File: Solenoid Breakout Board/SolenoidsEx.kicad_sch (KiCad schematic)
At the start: 80 parts, among them Q10 IRF540N, Q11 IRF540N, Q12 IRF540N, Q13 IRF540N, Q14 IRF540N, Q15 IRF540N, Q16 IRF540N, Q17 IRF540N, Q18 IRF540N, Q19 IRF540N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

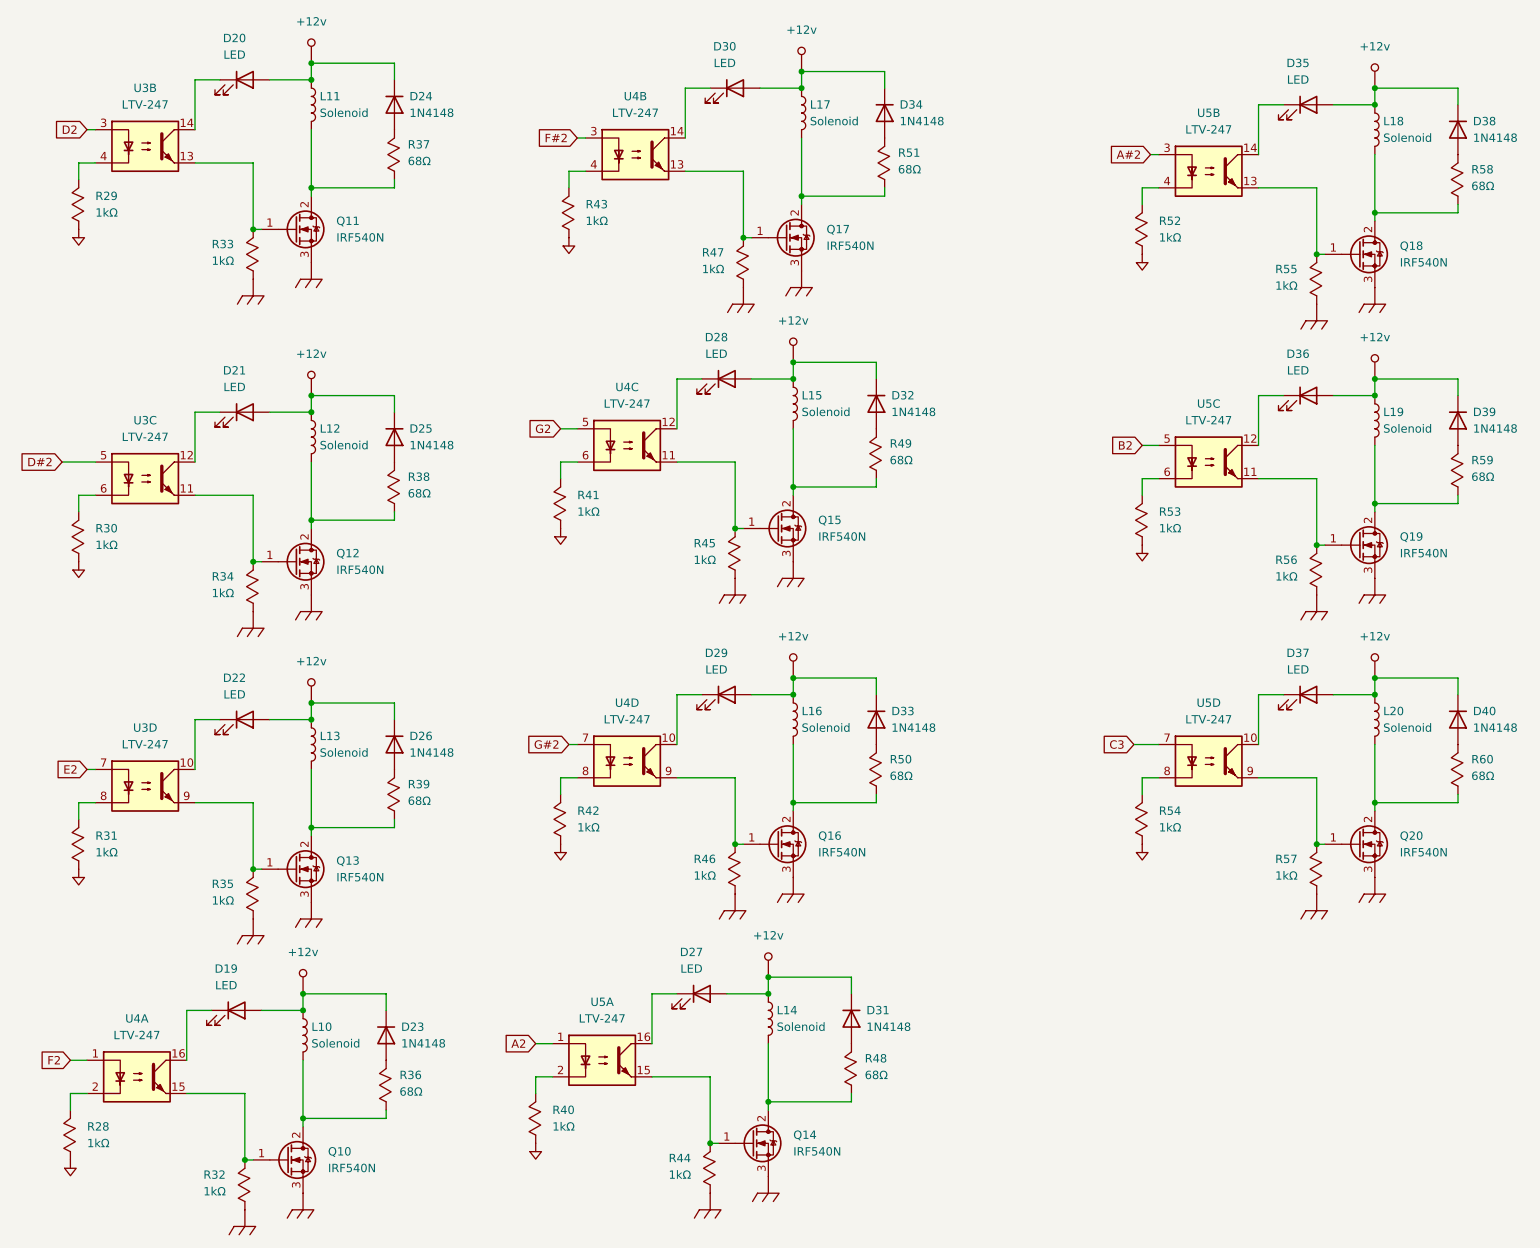
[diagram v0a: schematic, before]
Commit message: replaced footprints on breakout to match new components
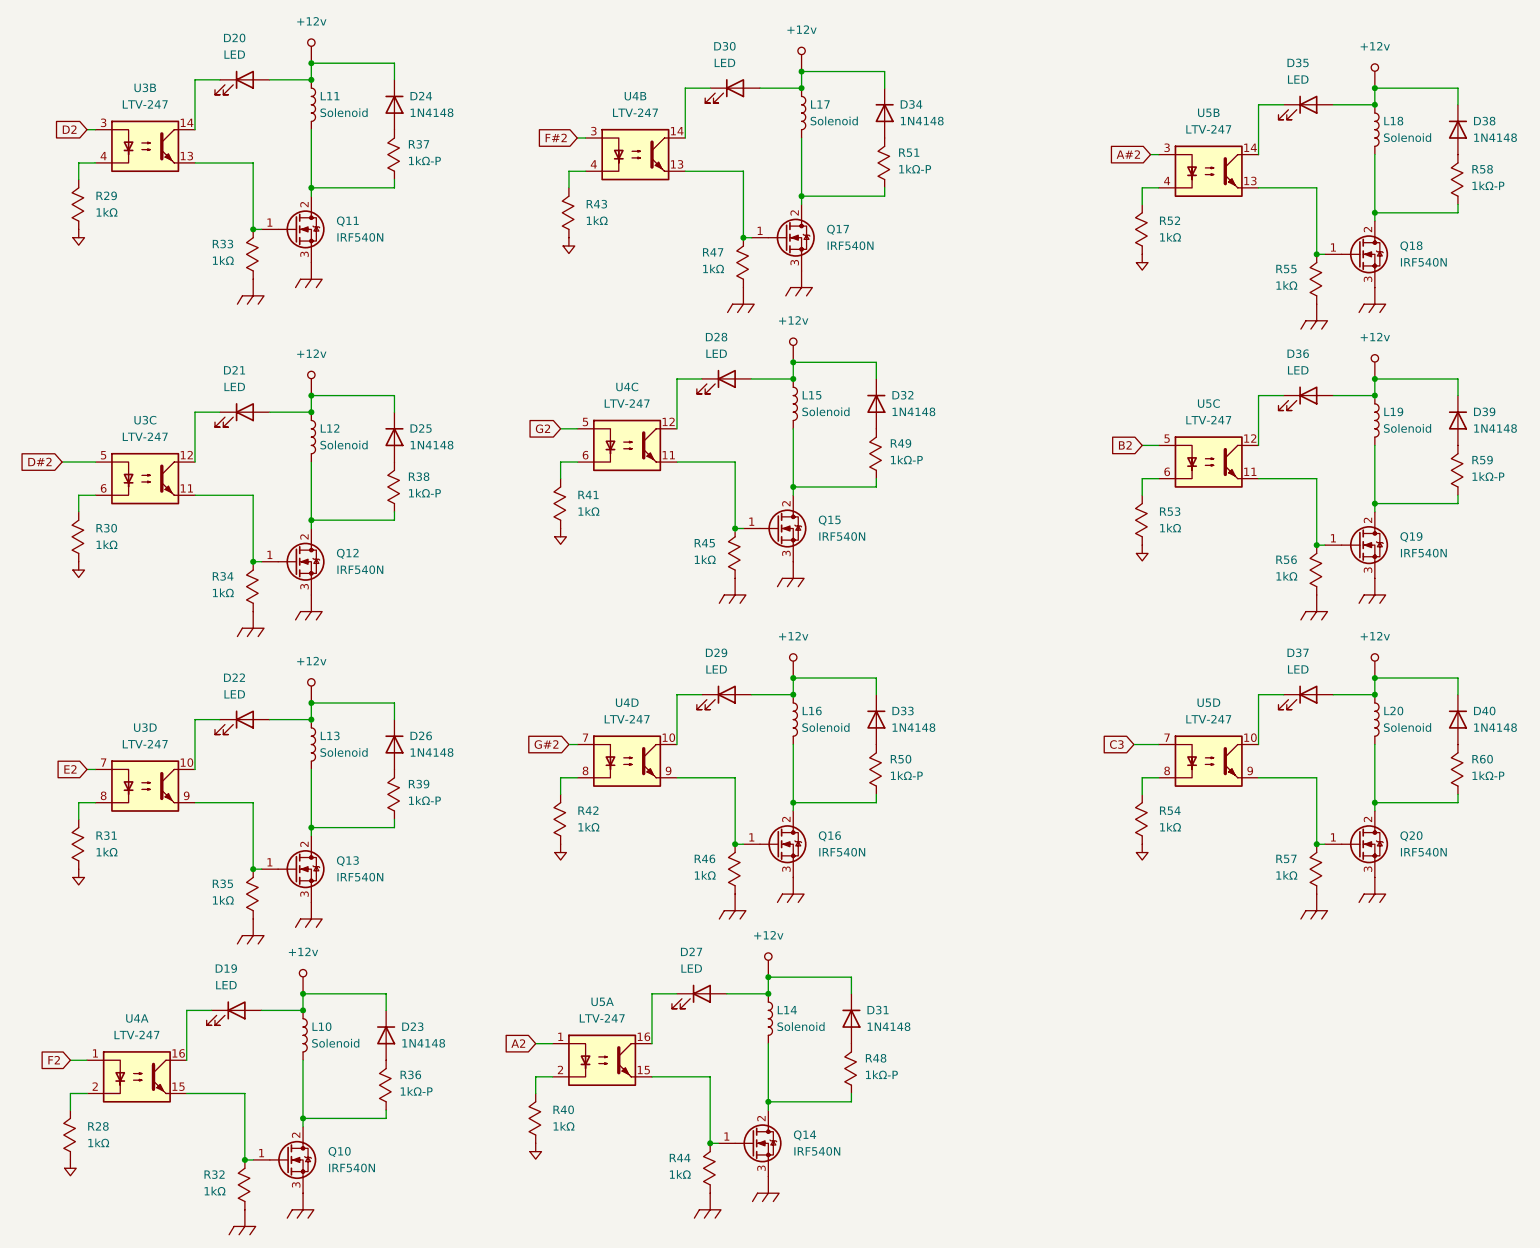
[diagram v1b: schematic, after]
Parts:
- Q10, Q11, Q12, Q13, Q14, Q15, Q16, Q17, Q18, Q19, Q20: footprint Package_TO_SOT_THT:TO-220-3_Vertical -> Package_TO_SOT_THT:TO-220-3_Horizontal_TabUp
- R36, R37, R38, R39, R48, R49, R50, R51, R58, R59, R60: value 68Ω -> 1kΩ-P; footprint Resistor_SMD:R_0805_2012Metric_Pad1.20x1.40mm_HandSolder -> Resistor_SMD:R_1206_3216Metric_Pad1.30x1.75mm_HandSolder
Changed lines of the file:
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@@
 			)
 		)
-		(property "Value" "68Ω"
+		(property "Value" "1kΩ-P"
 			(at 71.882 180.086 90)
 			(effects
@@
 			)
 		)
-		(property "Footprint" "Resistor_SMD:R_0805_2012Metric_Pad1.20x1.40mm_HandSolder"
+		(property "Footprint" "Resistor_SMD:R_1206_3216Metric_Pad1.30x1.75mm_HandSolder"
 			(at 67.31 180.34 0)
 			(effects
@@
 			)
 		)
-		(property "Footprint" "Package_TO_SOT_THT:TO-220-3_Vertical"
+		(property "Footprint" "Package_TO_SOT_THT:TO-220-3_Horizontal_TabUp"
 			(at 134.62 95.885 0)
 			(effects
@@
 			)
 		)
-		(property "Value" "68Ω"
+		(property "Value" "1kΩ-P"
 			(at 73.152 37.846 90)
 			(effects
@@
 			)
 		)
-		(property "Footprint" "Resistor_SMD:R_0805_2012Metric_Pad1.20x1.40mm_HandSolder"
+		(property "Footprint" "Resistor_SMD:R_1206_3216Metric_Pad1.30x1.75mm_HandSolder"
 			(at 68.58 38.1 0)
 			(effects
@@
 			)
 		)
-		(property "Value" "68Ω"
+		(property "Value" "1kΩ-P"
 			(at 146.812 83.566 90)
 			(effects
@@
 			)
 		)
-		(property "Footprint" "Resistor_SMD:R_0805_2012Metric_Pad1.20x1.40mm_HandSolder"
+		(property "Footprint" "Resistor_SMD:R_1206_3216Metric_Pad1.30x1.75mm_HandSolder"
 			(at 142.24 83.82 0)
 			(effects
@@
 			)
 		)
-		(property "Value" "68Ω"
+		(property "Value" "1kΩ-P"
 			(at 146.812 131.826 90)
 			(effects
@@
 			)
 		)
-		(property "Footprint" "Resistor_SMD:R_0805_2012Metric_Pad1.20x1.40mm_HandSolder"
+		(property "Footprint" "Resistor_SMD:R_1206_3216Metric_Pad1.30x1.75mm_HandSolder"
 			(at 142.24 132.08 0)
 			(effects
@@
 			)
 		)
-		(property "Value" "68Ω"
+		(property "Value" "1kΩ-P"
 			(at 235.712 86.106 90)
 			(effects
@@
 			)
 		)
-		(property "Footprint" "Resistor_SMD:R_0805_2012Metric_Pad1.20x1.40mm_HandSolder"
+		(property "Footprint" "Resistor_SMD:R_1206_3216Metric_Pad1.30x1.75mm_HandSolder"
 			(at 231.14 86.36 0)
 			(effects
@@
 			)
 		)
-		(property "Value" "68Ω"
+		(property "Value" "1kΩ-P"
 			(at 235.712 41.656 90)
 			(effects
@@
 			)
 		)
-		(property "Footprint" "Resistor_SMD:R_0805_2012Metric_Pad1.20x1.40mm_HandSolder"
+		(property "Footprint" "Resistor_SMD:R_1206_3216Metric_Pad1.30x1.75mm_HandSolder"
 			(at 231.14 41.91 0)
 			(effects
@@
 			)
 		)
-		(property "Footprint" "Package_TO_SOT_THT:TO-220-3_Vertical"
+		(property "Footprint" "Package_TO_SOT_THT:TO-220-3_Horizontal_TabUp"
 			(at 130.81 189.865 0)
 			(effects
@@
 			)
 		)
-		(property "Footprint" "Package_TO_SOT_THT:TO-220-3_Vertical"
+		(property "Footprint" "Package_TO_SOT_THT:TO-220-3_Horizontal_TabUp"
 			(at 60.96 50.165 0)
 			(effects
@@
 			)
 		)
-		(property "Value" "68Ω"
+		(property "Value" "1kΩ-P"
 			(at 148.082 39.116 90)
 			(effects
@@
 			)
 		)
-		(property "Footprint" "Resistor_SMD:R_0805_2012Metric_Pad1.20x1.40mm_HandSolder"
+		(property "Footprint" "Resistor_SMD:R_1206_3216Metric_Pad1.30x1.75mm_HandSolder"
 			(at 143.51 39.37 0)
 			(effects
@@
 			)
 		)
-		(property "Footprint" "Package_TO_SOT_THT:TO-220-3_Vertical"
+		(property "Footprint" "Package_TO_SOT_THT:TO-220-3_Horizontal_TabUp"
 			(at 223.52 53.975 0)
 			(effects
@@
 			)
 		)
-		(property "Footprint" "Package_TO_SOT_THT:TO-220-3_Vertical"
+		(property "Footprint" "Package_TO_SOT_THT:TO-220-3_Horizontal_TabUp"
 			(at 223.52 98.425 0)
 			(effects
@@
 			)
 		)
-		(property "Footprint" "Package_TO_SOT_THT:TO-220-3_Vertical"
+		(property "Footprint" "Package_TO_SOT_THT:TO-220-3_Horizontal_TabUp"
 			(at 60.96 147.955 0)
 			(effects
@@
 			)
 		)
-		(property "Value" "68Ω"
+		(property "Value" "1kΩ-P"
 			(at 143.002 177.546 90)
 			(effects
@@
 			)
 		)
-		(property "Footprint" "Resistor_SMD:R_0805_2012Metric_Pad1.20x1.40mm_HandSolder"
+		(property "Footprint" "Resistor_SMD:R_1206_3216Metric_Pad1.30x1.75mm_HandSolder"
 			(at 138.43 177.8 0)
 			(effects
@@
 			)
 		)
-		(property "Value" "68Ω"
+		(property "Value" "1kΩ-P"
 			(at 73.152 135.636 90)
 			(effects
@@
 			)
 		)
-		(property "Footprint" "Resistor_SMD:R_0805_2012Metric_Pad1.20x1.40mm_HandSolder"
+		(property "Footprint" "Resistor_SMD:R_1206_3216Metric_Pad1.30x1.75mm_HandSolder"
 			(at 68.58 135.89 0)
 			(effects
@@
 			)
 		)
-		(property "Footprint" "Package_TO_SOT_THT:TO-220-3_Vertical"
+		(property "Footprint" "Package_TO_SOT_THT:TO-220-3_Horizontal_TabUp"
 			(at 60.96 100.965 0)
 			(effects
@@
 			)
 		)
-		(property "Footprint" "Package_TO_SOT_THT:TO-220-3_Vertical"
+		(property "Footprint" "Package_TO_SOT_THT:TO-220-3_Horizontal_TabUp"
 			(at 59.69 192.405 0)
 			(effects
@@
 			)
 		)
-		(property "Footprint" "Package_TO_SOT_THT:TO-220-3_Vertical"
+		(property "Footprint" "Package_TO_SOT_THT:TO-220-3_Horizontal_TabUp"
 			(at 134.62 144.145 0)
 			(effects
@@
 			)
 		)
-		(property "Footprint" "Package_TO_SOT_THT:TO-220-3_Vertical"
+		(property "Footprint" "Package_TO_SOT_THT:TO-220-3_Horizontal_TabUp"
 			(at 135.89 51.435 0)
 			(effects
@@
 			)
 		)
-		(property "Footprint" "Package_TO_SOT_THT:TO-220-3_Vertical"
+		(property "Footprint" "Package_TO_SOT_THT:TO-220-3_Horizontal_TabUp"
 			(at 223.52 144.145 0)
 			(effects
@@
 			)
 		)
-		(property "Value" "68Ω"
+		(property "Value" "1kΩ-P"
 			(at 235.712 131.826 90)
 			(effects
@@
 			)
 		)
-		(property "Footprint" "Resistor_SMD:R_0805_2012Metric_Pad1.20x1.40mm_HandSolder"
+		(property "Footprint" "Resistor_SMD:R_1206_3216Metric_Pad1.30x1.75mm_HandSolder"
 			(at 231.14 132.08 0)
 			(effects
@@
 			)
 		)
-		(property "Value" "68Ω"
+		(property "Value" "1kΩ-P"
 			(at 73.152 88.646 90)
 			(effects
@@
 			)
 		)
-		(property "Footprint" "Resistor_SMD:R_0805_2012Metric_Pad1.20x1.40mm_HandSolder"
+		(property "Footprint" "Resistor_SMD:R_1206_3216Metric_Pad1.30x1.75mm_HandSolder"
 			(at 68.58 88.9 0)
 			(effects
